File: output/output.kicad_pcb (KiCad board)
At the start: 2 copper layers, 25.4 x 25.4 mm, 28 parts, among them J1 PPS IO, J2 Power Input, J3 Output, Q1 BSS138, Q2 BSS138, U1 OPA2990, U2 SN74LVC1G3157, U3 INA2181, U4 SN74LVC1G3157

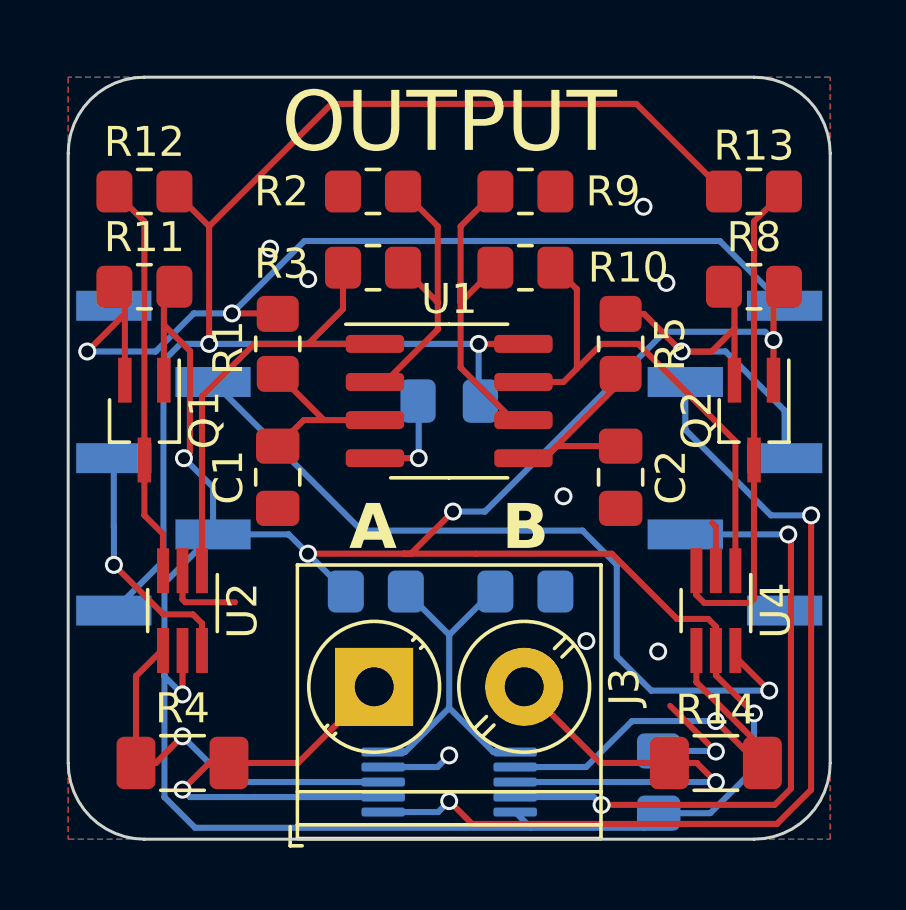
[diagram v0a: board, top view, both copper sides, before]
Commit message: Address review comments, finish routing HILT main board
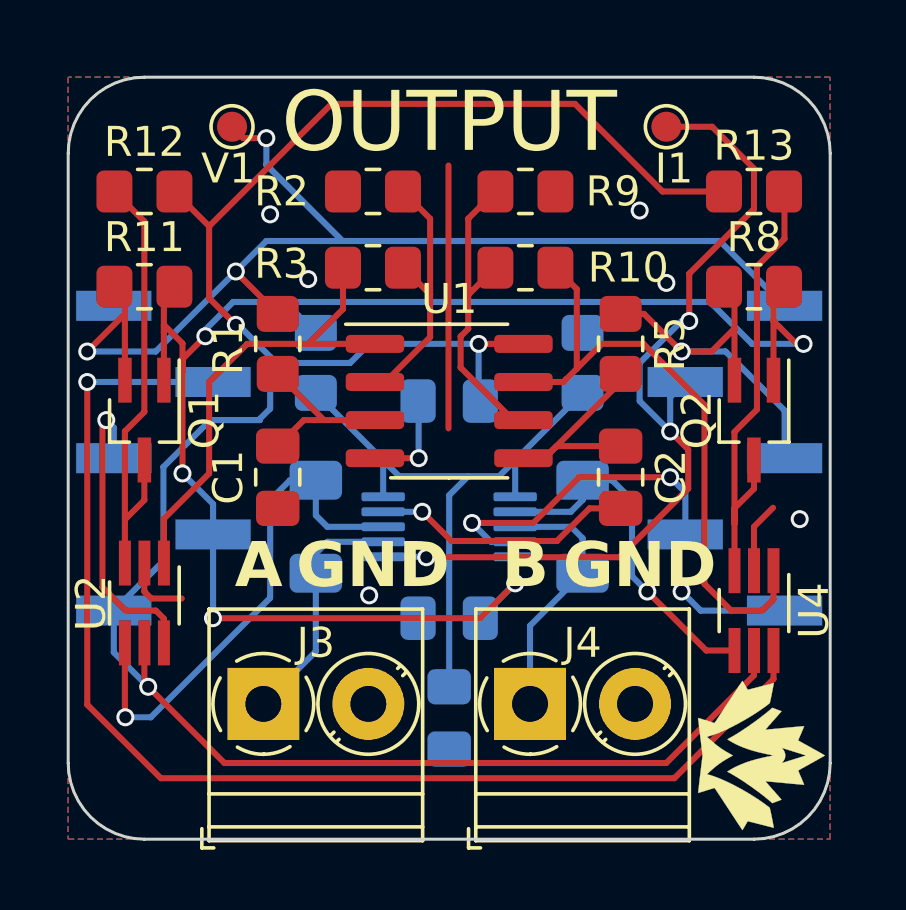
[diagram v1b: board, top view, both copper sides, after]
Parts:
- added C5: 100n, Capacitor_SMD:C_0805_2012Metric_Pad1.18x1.45mm_HandSolder, B.Cu at (114.9, 103.9)
- added G***: LOGO, Team_Logo:Logo_SilkScreen_5mm, F.Cu at (125.3, 105.2)
- added J4: Output B, TerminalBlock_Phoenix:TerminalBlock_Phoenix_PT-1,5-2-3.5-H_1x02_P3.50mm_Horizontal, F.Cu at (117.6, 103.4)
- added TP1: V1, TestPoint:TestPoint_Pad_D1.0mm, F.Cu at (107.7, 84.2)
- added TP2: I1, TestPoint:TestPoint_Pad_D1.0mm, F.Cu at (122.2, 84.2)
- J3: value Output -> Output A; footprint TerminalBlock_Phoenix:TerminalBlock_Phoenix_PT-1,5-2-5.0-H_1x02_P5.00mm_Horizontal -> TerminalBlock_Phoenix:TerminalBlock_Phoenix_PT-1,5-2-3.5-H_1x02_P3.50mm_Horizontal
- R12, R13: value 10k -> 1k
- R14, R4: value 20mR -> 150mR; moved to B.Cu
- moved R14 9.04 mm to (119.4, 97.5), turned to -90 degrees
- moved R4 9.04 mm to (110.5, 97.5), turned to -90 degrees
- moved C4 8.87 mm to (114.9, 100.6), turned to 180 degrees
- moved U3 8.51 mm to (114.9, 97.5)
- moved R6 7.88 mm to (110.5, 92.1), turned to 90 degrees
- moved R7 7.85 mm to (119.4, 92.1), turned to 90 degrees
- moved J3 3.74 mm to (108.7, 103.4)
- moved U2 1.30 mm to (104.8, 100.1)
- moved U4 1.27 mm to (125.1, 100.3)
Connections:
- J3 pad 2: /OUT2 -> GND
- U2 pad 5: +3V3 -> +5V
- U4 pad 5: +3V3 -> +5V
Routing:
- net +3V3: track 88.4 -> 55.7 mm, vias 6 -> 5
- net +5V: track 48.8 -> 77.1 mm, vias 2 -> 3
- net GND: track 14.3 -> 29.3 mm, vias 10 -> 9
- net /A~{D}2: track 26.4 -> 41.2 mm
- net /I2: track 21.5 -> 11.0 mm
- net /REF: track 12.2 -> 20.9 mm
- net /OUT1: track 14.6 -> 8.15 mm, vias 1 -> 0
- net /V1: track 32.2 -> 38.5 mm, vias 2 -> 3
- net /OUT2: track 14.4 -> 8.65 mm, vias 1 -> 0
- net /I1+: track 13.4 -> 17.6 mm
- net /OUT2A: track 16.9 -> 20.8 mm
- net /I2+: track 14.1 -> 12.0 mm
- net /A~{D}1: track 8.20 -> 10.3 mm
- net /OUT1D: track 13.3 -> 15.3 mm
- net /I1: track 31.3 -> 29.5 mm, vias 2 -> 3
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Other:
- board text added: "2023/ 04/30"
- board text added: "GND"
- board text removed: "2022/ 04/22"

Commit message: Address review comments
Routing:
- net +3V3: track 55.7 -> 55.1 mm
- net GND: vias 9 -> 12
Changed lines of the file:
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@@
   (segment (start 105.0026 99.9268) (end 106.0228 99.9268) (width 0.2032) (layer "F.Cu") (net 2))
   (segment (start 125.095 97.536) (end 125.73 96.901) (width 0.2032) (layer "F.Cu") (net 2))
+  (via (at 114.935 94.869) (size 0.8) (drill 0.4) (layers "F.Cu" "B.Cu") (free) (net 2))
   (via (at 122.682 99.695) (size 0.6) (drill 0.4) (layers "F.Cu" "B.Cu") (net 2))
   (via (at 114.038 97.036) (size 0.6) (drill 0.4) (layers "F.Cu" "B.Cu") (net 2))
@@
   (via (at 108.966 87.122) (size 0.6) (drill 0.4) (layers "F.Cu" "B.Cu") (net 2))
   (via (at 113.919 95.25) (size 0.6) (drill 0.4) (layers "F.Cu" "B.Cu") (net 2))
-  (via (at 122.174 89.408) (size 0.6) (drill 0.4) (layers "F.Cu" "B.Cu") (net 2))
-  (via (at 110.236 89.281) (size 0.6) (drill 0.4) (layers "F.Cu" "B.Cu") (net 2))
+  (via (at 111.633 84.836) (size 0.8) (drill 0.4) (layers "F.Cu" "B.Cu") (free) (net 2))
+  (via (at 121.412 88.9) (size 0.6) (drill 0.4) (layers "F.Cu" "B.Cu") (net 2))
+  (via (at 109.601 88.9) (size 0.6) (drill 0.4) (layers "F.Cu" "B.Cu") (net 2))
   (via (at 126.619 97.282) (size 0.6) (drill 0.4) (layers "F.Cu" "B.Cu") (free) (net 2))
-  (via (at 112.268 99.822) (size 0.6) (drill 0.4) (layers "F.Cu" "B.Cu") (free) (net 2))
+  (via (at 112.522 99.568) (size 0.6) (drill 0.4) (layers "F.Cu" "B.Cu") (free) (net 2))
+  (via (at 126.746 103.505) (size 0.8) (drill 0.4) (layers "F.Cu" "B.Cu") (free) (net 2))
   (segment (start 113.919 95.25) (end 113.919 93.3665) (width 0.2032) (layer "B.Cu") (net 2))
   (segment (start 122.682 99.695) (end 123.317 100.33) (width 0.2032) (layer "B.Cu") (net 2))
@@
   (segment (start 108.6216 93.98) (end 108.6216 93.9434) (width 0.2032) (layer "B.Cu") (net 8))
   (segment (start 108.6216 93.9434) (end 108.966 93.599) (width 0.2032) (layer "B.Cu") (net 8))
+  (segment (start 108.712 100.584) (end 107.95 99.822) (width 0.2032) (layer "F.Cu") (net 9))
   (segment (start 126.746 91.44) (end 126.507 91.44) (width 0.2032) (layer "F.Cu") (net 9))
   (segment (start 105.425 91.059) (end 105.425 92.65) (width 0.2032) (layer "F.Cu") (net 9))
@@
   (segment (start 125.745 92.65) (end 125.745 90.678) (width 0.2032) (layer "F.Cu") (net 9))
   (segment (start 126.507 91.44) (end 125.745 90.678) (width 0.2032) (layer "F.Cu") (net 9))
-  (segment (start 107.061 100.584) (end 115.9725 100.584) (width 0.2032) (layer "F.Cu") (net 9))
+  (segment (start 117.135 100.584) (end 108.712 100.584) (width 0.2032) (layer "F.Cu") (net 9))
   (segment (start 105.425 89.885) (end 105.425 91.059) (width 0.2032) (layer "F.Cu") (net 9))
   (segment (start 106.807 91.186) (end 106.045 91.948) (width 0.2032) (layer "F.Cu") (net 9))
-  (segment (start 115.9725 100.584) (end 117.135 99.4215) (width 0.2032) (layer "F.Cu") (net 9))
   (segment (start 105.425 90.805) (end 105.425 91.059) (width 0.2032) (layer "F.Cu") (net 9))
   (segment (start 105.775 89.535) (end 105.425 89.885) (width 0.2032) (layer "F.Cu") (net 9))
@@
   (via (at 106.045 95.758) (size 0.6) (drill 0.4) (layers "F.Cu" "B.Cu") (net 9))
   (via (at 126.746 91.44) (size 0.6) (drill 0.4) (layers "F.Cu" "B.Cu") (net 9))
-  (via (at 117.135 99.4215) (size 0.6) (drill 0.4) (layers "F.Cu" "B.Cu") (net 9))
+  (via (at 117.135 100.584) (size 0.6) (drill 0.4) (layers "F.Cu" "B.Cu") (net 9))
   (via (at 106.807 91.186) (size 0.6) (drill 0.4) (layers "F.Cu" "B.Cu") (net 9))
-  (via (at 107.061 100.584) (size 0.6) (drill 0.4) (layers "F.Cu" "B.Cu") (net 9))
+  (via (at 107.95 99.822) (size 0.6) (drill 0.4) (layers "F.Cu" "B.Cu") (net 9))
   (segment (start 110.49 91.075) (end 109.458 90.043) (width 0.2032) (layer "B.Cu") (net 9))
-  (segment (start 125.0268 91.44) (end 126.746 91.44) (width 0.2032) (layer "B.Cu") (net 9))
   (segment (start 106.045 95.758) (end 107.065 96.778) (width 0.2032) (layer "B.Cu") (net 9))
-  (segment (start 109.7788 90.043) (end 107.734209 90.043) (width 0.2032) (layer "B.Cu") (net 9))
-  (segment (start 107.734209 90.043) (end 106.807 90.970209) (width 0.2032) (layer "B.Cu") (net 9))
-  (segment (start 117.135 99.4215) (end 115.9725 100.584) (width 0.2032) (layer "B.Cu") (net 9))
-  (segment (start 107.065 97.79) (end 107.065 100.58) (width 0.2032) (layer "B.Cu") (net 9))
-  (segment (start 107.065 100.58) (end 107.061 100.584) (width 0.2032) (layer "B.Cu") (net 9))
+  (segment (start 117.135 100.584) (end 115.9725 100.584) (width 0.2032) (layer "B.Cu") (net 9))
+  (segment (start 124.745105 91.636314) (end 126.549686 91.636314) (width 0.2032) (layer "B.Cu") (net 9))
+  (segment (start 107.065 98.937) (end 107.065 97.79) (width 0.2032) (layer "B.Cu") (net 9))
+  (segment (start 126.549686 91.636314) (end 126.746 91.44) (width 0.2032) (layer "B.Cu") (net 9))
+  (segment (start 106.807 91.186) (end 106.807 90.970209) (width 0.2032) (layer "B.Cu") (net 9))
   (segment (start 107.065 96.778) (end 107.065 97.79) (width 0.2032) (layer "B.Cu") (net 9))
-  (segment (start 117.135 98.536) (end 117.135 99.4215) (width 0.2032) (layer "B.Cu") (net 9))
-  (segment (start 109.7788 90.043) (end 123.6298 90.043) (width 0.2032) (layer "B.Cu") (net 9))
-  (segment (start 123.6298 90.043) (end 125.0268 91.44) (width 0.2032) (layer "B.Cu") (net 9))
-  (segment (start 106.807 90.970209) (end 106.807 91.186) (width 0.2032) (layer "B.Cu") (net 9))
+  (segment (start 107.95 99.822) (end 107.065 98.937) (width 0.2032) (layer "B.Cu") (net 9))
+  (segment (start 106.807 90.970209) (end 107.734209 90.043) (width 0.2032) (layer "B.Cu") (net 9))
+  (segment (start 117.135 98.536) (end 117.135 100.584) (width 0.2032) (layer "B.Cu") (net 9))
+  (segment (start 123.151791 90.043) (end 124.745105 91.636314) (width 0.2032) (layer "B.Cu") (net 9))
+  (segment (start 107.734209 90.043) (end 123.151791 90.043) (width 0.2032) (layer "B.Cu") (net 9))
   (segment (start 104.775 93.704895) (end 104.125 94.354895) (width 0.2032) (layer "F.Cu") (net 10))
   (segment (start 103.775 86.36) (end 104.775 87.36) (width 0.2032) (layer "F.Cu") (net 10))
@@
   (segment (start 110.879 98.036) (end 110.49 98.425) (width 0.2032) (layer "B.Cu") (net 12))
   (segment (start 112.735 98.036) (end 110.879 98.036) (width 0.2032) (layer "B.Cu") (net 12))
+  (segment (start 119.38 101.727) (end 119.38 99.086) (width 0.2032) (layer "B.Cu") (net 13))
   (segment (start 118.999 97.536) (end 119.38 97.917) (width 0.2032) (layer "B.Cu") (net 13))
+  (segment (start 117.63 103.44) (end 117.667 103.44) (width 0.2032) (layer "B.Cu") (net 13))
   (segment (start 119.38 97.917) (end 119.38 99.086) (width 0.2032) (layer "B.Cu") (net 13))
-  (segment (start 117.63 103.44) (end 117.63 100.836) (width 0.2032) (layer "B.Cu") (net 13))
-  (segment (start 117.63 100.836) (end 119.38 99.086) (width 0.2032) (layer "B.Cu") (net 13))
   (segment (start 117.135 97.536) (end 118.999 97.536) (width 0.2032) (layer "B.Cu") (net 13))
+  (segment (start 117.667 103.44) (end 119.38 101.727) (width 0.2032) (layer "B.Cu") (net 13))
   (segment (start 114.3 91.213659) (end 112.803659 92.71) (width 0.2032) (layer "F.Cu") (net 14))
   (segment (start 113.395 88.9) (end 113.411 88.9) (width 0.2032) (layer "F.Cu") (net 14))
@@
   (segment (start 115.57 87.265) (end 116.475 86.36) (width 0.2032) (layer "F.Cu") (net 17))
   (segment (start 117.41 93.98) (end 117.066341 93.98) (width 0.2032) (layer "F.Cu") (net 17))
-  (segment (start 121.539 99.695) (end 123.504 101.66) (width 0.2032) (layer "F.Cu") (net 18))
-  (segment (start 123.504 101.66) (end 124.445 101.66) (width 0.2032) (layer "F.Cu") (net 18))
-  (via (at 121.539 99.695) (size 0.6) (drill 0.4) (layers "F.Cu" "B.Cu") (net 18))
+  (segment (start 123.25 101.66) (end 124.445 101.66) (width 0.2032) (layer "F.Cu") (net 18))
+  (segment (start 122.428 100.838) (end 123.25 101.66) (width 0.2032) (layer "F.Cu") (net 18))
+  (via (at 122.428 100.838) (size 0.6) (drill 0.4) (layers "F.Cu" "B.Cu") (net 18))
   (segment (start 119.38 96.647) (end 119.38 95.986) (width 0.2032) (layer "B.Cu") (net 18))
+  (segment (start 121.031 96.647) (end 120.37 95.986) (width 0.2032) (layer "B.Cu") (net 18))
   (segment (start 117.135 97.036) (end 118.991 97.036) (width 0.2032) (layer "B.Cu") (net 18))
+  (segment (start 120.37 95.986) (end 119.38 95.986) (width 0.2032) (layer "B.Cu") (net 18))
+  (segment (start 122.428 100.838) (end 121.031 99.441) (width 0.2032) (layer "B.Cu") (net 18))
   (segment (start 118.991 97.036) (end 119.38 96.647) (width 0.2032) (layer "B.Cu") (net 18))
-  (segment (start 121.539 99.695) (end 121.031 99.187) (width 0.2032) (layer "B.Cu") (net 18))
-  (segment (start 121.031 99.187) (end 121.031 96.647) (width 0.2032) (layer "B.Cu") (net 18))
-  (segment (start 121.031 96.647) (end 120.37 95.986) (width 0.2032) (layer "B.Cu") (net 18))
-  (segment (start 120.37 95.986) (end 119.38 95.986) (width 0.2032) (layer "B.Cu") (net 18))
+  (segment (start 121.031 99.441) (end 121.031 96.647) (width 0.2032) (layer "B.Cu") (net 18))
   (segment (start 110.0875 93.98) (end 110.76 93.98) (width 0.2032) (layer "F.Cu") (net 19))
   (segment (start 112.46 93.98) (end 110.76 93.98) (width 0.2032) (layer "F.Cu") (net 19))
